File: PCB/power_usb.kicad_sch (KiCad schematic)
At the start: 29 parts, among them J1 USB_C_Receptacle, U1 LP2985-3.3, U3 CP2102N-A02-GQFN24, U5 LP2985-3.3

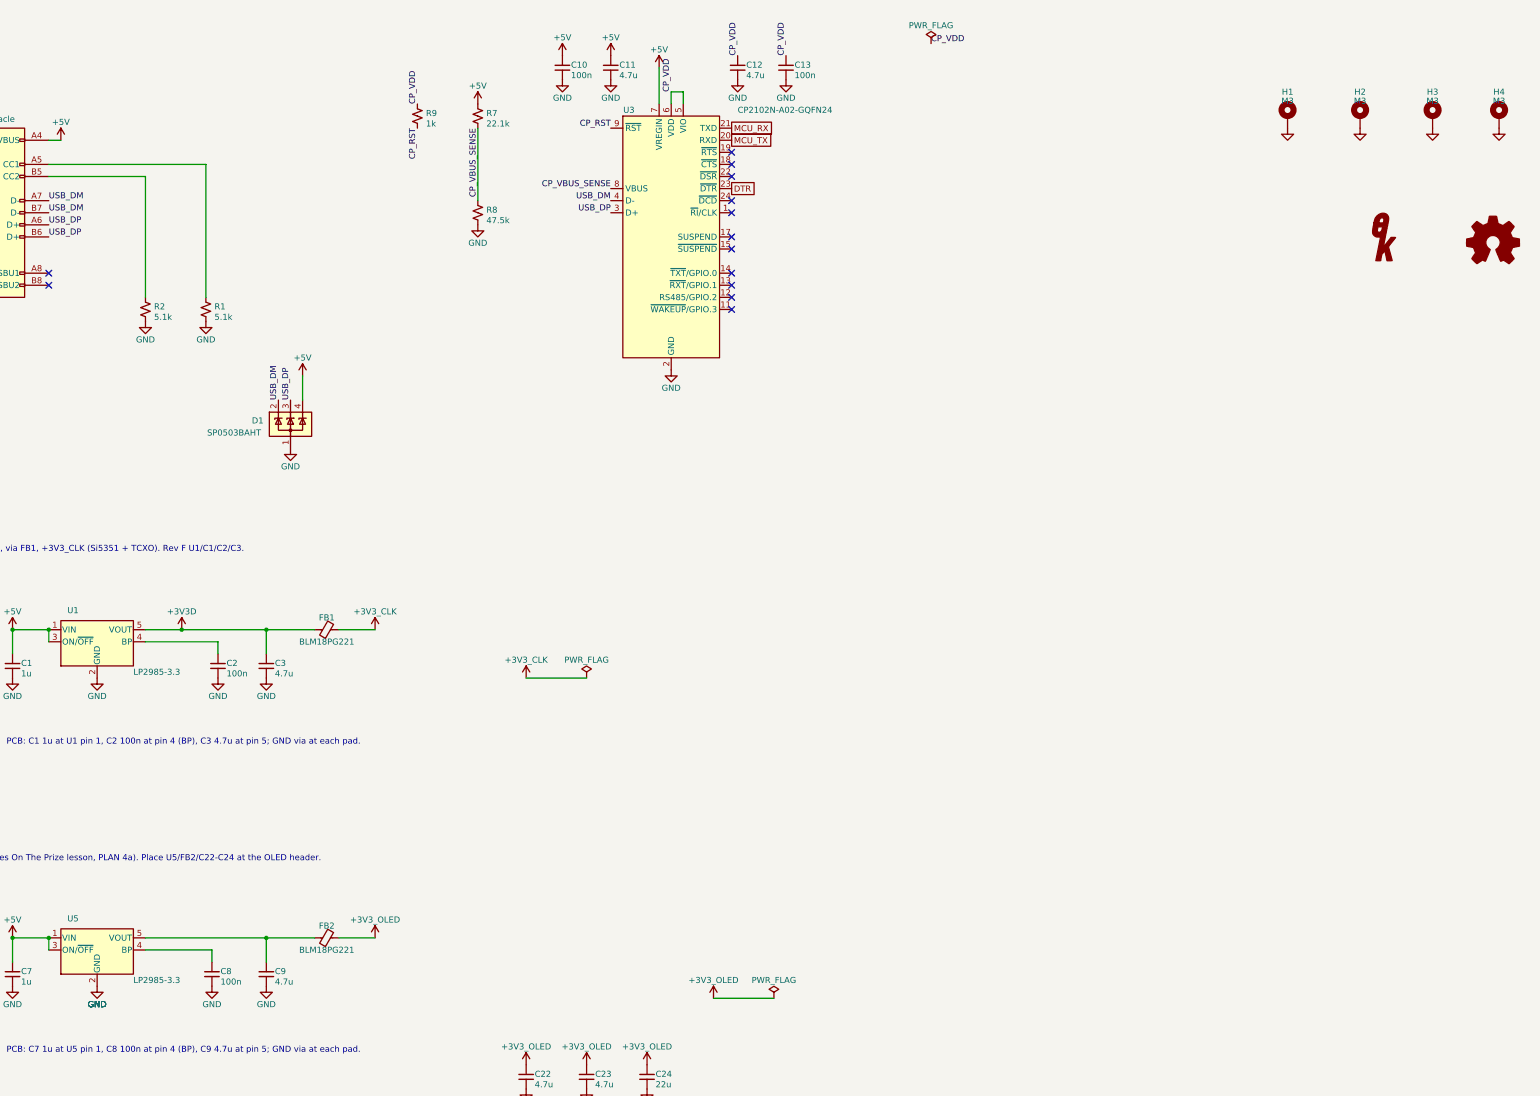
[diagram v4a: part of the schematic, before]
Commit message: SH1: DNP RF shield solder fence (GND), OSHW logo footprint
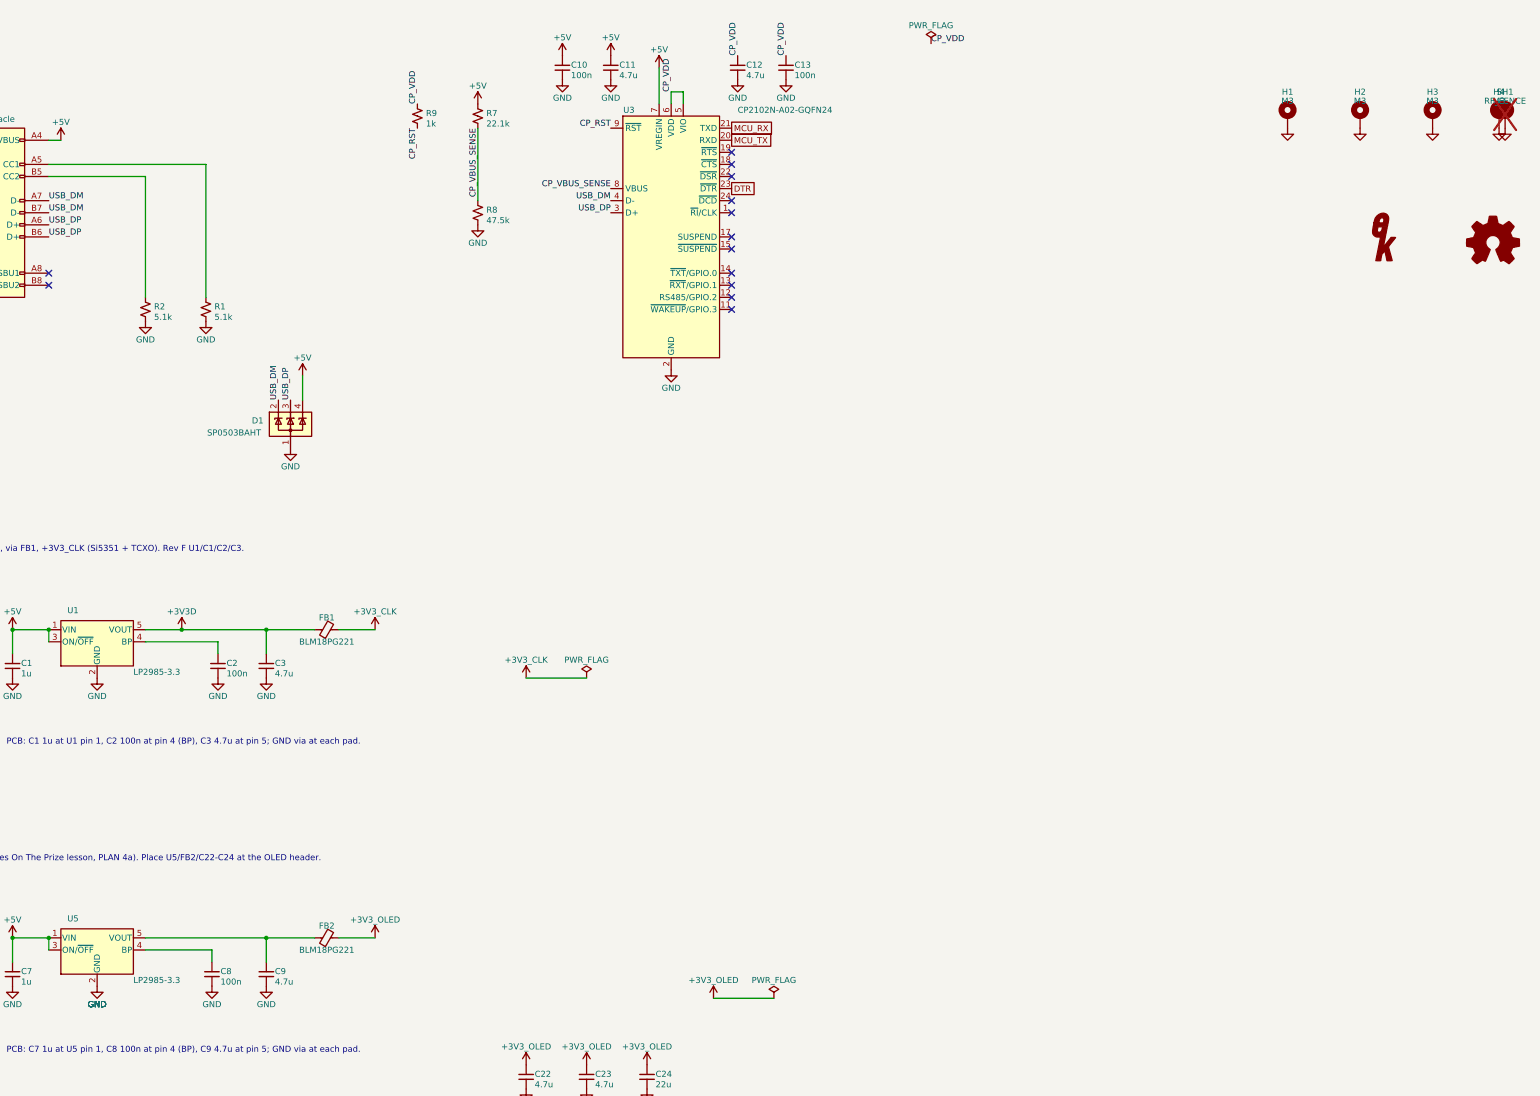
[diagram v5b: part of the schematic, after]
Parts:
- added SH1: RF_FENCE, EtherkitKicadLibrary:RF_Fence_42x33.5mm, symbol Mechanical:MountingHole_Pad
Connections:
- net GND: now also SH1.1
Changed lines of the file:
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@@
+	)
+	(symbol
+		(lib_id "Mechanical:MountingHole_Pad")
+		(at 365.76 59.69 0)
+		(unit 1)
+		(body_style 1)
+		(exclude_from_sim no)
+		(in_bom no)
+		(on_board yes)
+		(in_pos_files no)
+		(dnp yes)
+		(property "Reference" "SH1"
+			(at 365.76 54.61 0)
+			(show_name no)
+			(do_not_autoplace no)
+			(effects
+				(font
+					(size 1.27 1.27)
+				)
+			)
+		)
+		(property "Value" "RF_FENCE"
+			(at 365.76 56.515 0)
+			(show_name no)
+			(do_not_autoplace no)
+			(effects
+				(font
+					(size 1.27 1.27)
+				)
+			)
+		)
+		(property "Footprint" "EtherkitKicadLibrary:RF_Fence_42x33.5mm"
+			(at 365.76 59.69 0)
+			(hide yes)
+			(show_name no)
+			(do_not_autoplace no)
+			(effects
+				(font
+					(size 1.27 1.27)
+				)
+			)
+		)
+		(property "Datasheet" ""
+			(at 365.76 59.69 0)
+			(hide yes)
+			(show_name no)
+			(do_not_autoplace no)
+			(effects
+				(font
+					(size 1.27 1.27)
+				)
+			)
+		)
+		(property "Description" "DNP RF shield solder fence (42x33.5 mm, 1 mm GND strip) for a user-cut tin-plate can over Si5351/TCXO/LPFs; not in BOM"
+			(at 365.76 59.69 0)
+			(hide yes)
+			(show_name no)
+			(do_not_autoplace no)
+			(effects
+				(font
+					(size 1.27 1.27)
+				)
+			)
+		)
+		(pin "1"
+		)
+		(instances
+			(project "Si5351AVFO"
+				(path "/a0000000-0000-4000-8000-000000000001/b0000000-0000-4000-8000-000000000002"
+					(reference "SH1")
+					(unit 1)
+				)
+			)
+		)
+	)
+	(symbol
+		(lib_id "power:GND")
+		(at 365.76 62.23 0)
+		(unit 1)
+		(body_style 1)
+		(exclude_from_sim no)
+		(in_bom no)
+		(on_board yes)
+		(in_pos_files yes)
+		(dnp no)
+		(property "Reference" "#PWR910"
+			(at 365.76 62.23 0)
+			(hide yes)
+			(show_name no)
+			(do_not_autoplace no)
+			(effects
+				(font
+					(size 1.27 1.27)
+				)
+			)
+		)
+		(property "Value" "GND"
+			(at 69.85 246.38 0)
+			(show_name no)
+			(do_not_autoplace no)
+			(effects
+				(font
+					(size 1.27 1.27)
+				)
+			)
+		)
+		(property "Footprint" ""
+			(at 365.76 62.23 0)
+			(hide yes)
+			(show_name no)
+			(do_not_autoplace no)
+			(effects
+				(font
+					(size 1.27 1.27)
+				)
+			)
+		)
+		(property "Datasheet" ""
+			(at 365.76 62.23 0)
+			(hide yes)
+			(show_name no)
+			(do_not_autoplace no)
+			(effects
+				(font
+					(size 1.27 1.27)
+				)
+			)
+		)
+		(property "Description" ""
+			(at 365.76 62.23 0)
+			(show_name no)
+			(do_not_autoplace no)
+			(effects
+				(font
+					(size 1.27 1.27)
+				)
+			)
+		)
+		(pin "1"
+		)
+		(instances
+			(project "Si5351AVFO"
+				(path "/a0000000-0000-4000-8000-000000000001/b0000000-0000-4000-8000-000000000002"
+					(reference "#PWR910")
+					(unit 1)
+				)
+			)
+		)
 	)
 	(symbol

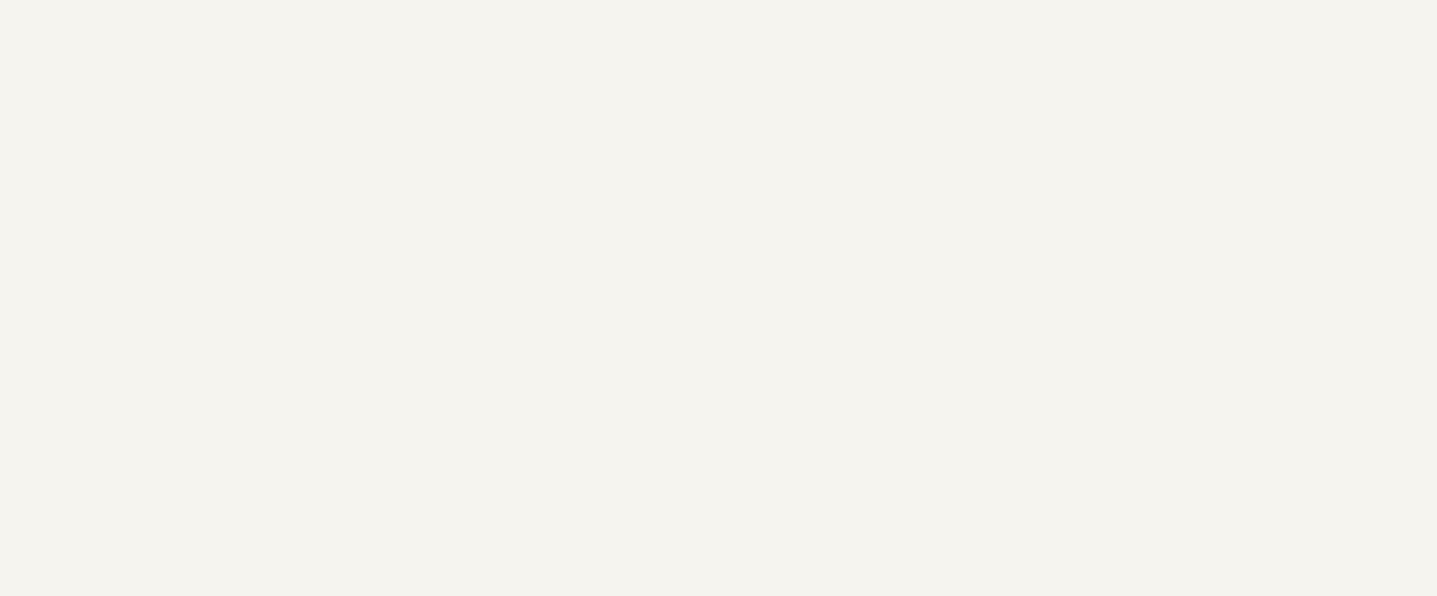
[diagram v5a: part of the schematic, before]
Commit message: Test points TP1-TP8 (GND x2, +5V, +3V3D, +3V3_CLK, +3V3_OLED, I2C_SCL/SDA) on B.Cu, 1.5 mm SMD, excluded from BOM/CPL; no RF nets. JLC fab outputs (tools/export_fab.sh -> PCB/production). ERC 0, DRC only the 15 accepted SMA edge hits
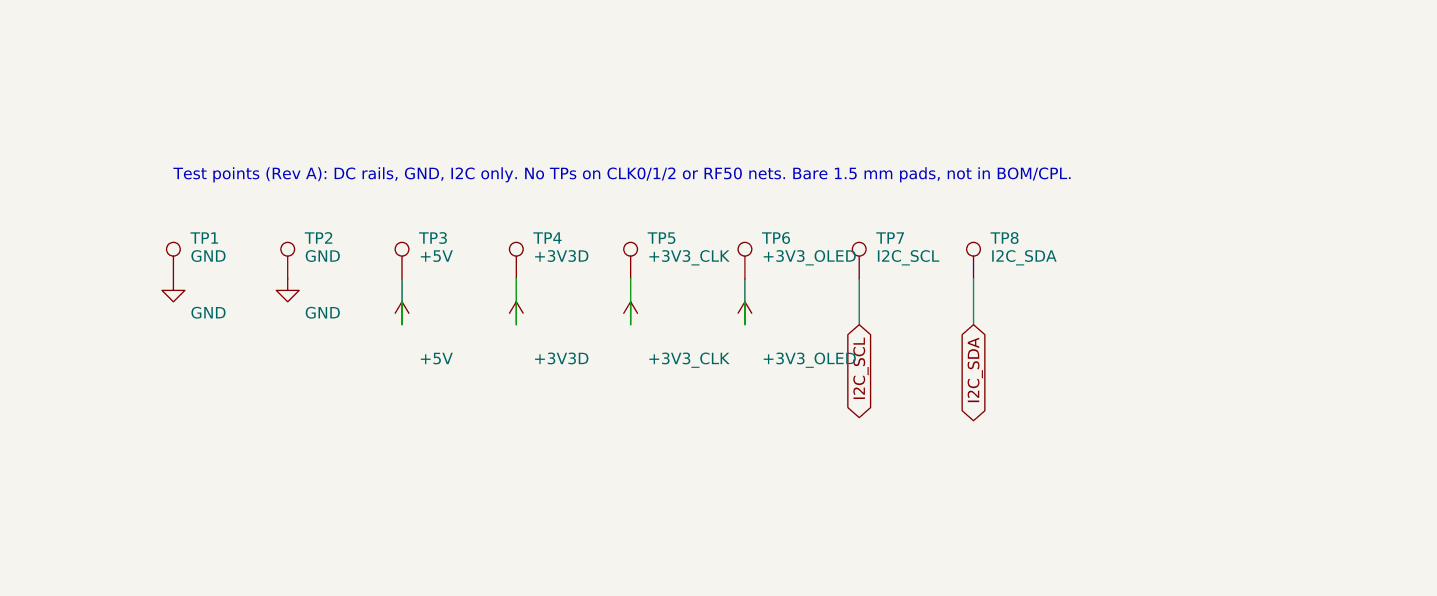
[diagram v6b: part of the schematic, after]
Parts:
- added TP1, TP2: GND, TestPoint:TestPoint_Pad_D1.5mm, symbol Connector:TestPoint
- added TP3: +5V, TestPoint:TestPoint_Pad_D1.5mm, symbol Connector:TestPoint
- added TP4: +3V3D, TestPoint:TestPoint_Pad_D1.5mm, symbol Connector:TestPoint
- added TP5: +3V3_CLK, TestPoint:TestPoint_Pad_D1.5mm, symbol Connector:TestPoint
- added TP6: +3V3_OLED, TestPoint:TestPoint_Pad_D1.5mm, symbol Connector:TestPoint
- added TP7: I2C_SCL, TestPoint:TestPoint_Pad_D1.5mm, symbol Connector:TestPoint
- added TP8: I2C_SDA, TestPoint:TestPoint_Pad_D1.5mm, symbol Connector:TestPoint
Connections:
- net +3V3D: now also TP4.1
- net +3V3_CLK: now also TP5.1
- net +3V3_OLED: now also TP6.1
- net +5V: now also TP3.1
- net GND: now also TP1.1, TP2.1
- new net I2C_SCL: TP7.1
- new net I2C_SDA: TP8.1
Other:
- note added: "Test points (Rev A): DC rails, GND, I2C only. No TPs on CLK0/1/2 or RF50 nets. Bare 1.5 mm pads, not in BOM/CPL."

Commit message: Basic-part swaps: C11/C12 C1705->C19666 (CL10A475KO8NNNC 16V), R1/R2 C105580->C23186 (0603WAF5101T5E). Board fields synced, ERC 0, DRC 15 accepted SMA hits, fab outputs + schematic PDF regenerated
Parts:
- C11, C12: LCSC C1705 -> C19666; MPN CL10A475KP8NNNC -> CL10A475KO8NNNC
- R1, R2: LCSC C105580 -> C23186; MPN RC0603FR-075K1L -> 0603WAF5101T5E; Manufacturer YAGEO -> UNI-ROYAL
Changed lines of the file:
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@@
 			)
 		)
-		(property "LCSC" "C1705"
+		(property "LCSC" "C19666"
 			(at 204.47 49.53 0)
 			(hide yes)
@@
 			)
 		)
-		(property "MPN" "CL10A475KP8NNNC"
+		(property "MPN" "CL10A475KO8NNNC"
 			(at 204.47 49.53 0)
 			(hide yes)
@@
 			)
 		)
-		(property "LCSC" "C1705"
+		(property "LCSC" "C19666"
 			(at 177.8 49.53 0)
 			(hide yes)
@@
 			)
 		)
-		(property "MPN" "CL10A475KP8NNNC"
+		(property "MPN" "CL10A475KO8NNNC"
 			(at 177.8 49.53 0)
 			(hide yes)
@@
 			)
 		)
-		(property "LCSC" "C105580"
+		(property "LCSC" "C23186"
 			(at 80.01 100.33 0)
 			(hide yes)
@@
 			)
 		)
-		(property "MPN" "RC0603FR-075K1L"
+		(property "MPN" "0603WAF5101T5E"
 			(at 80.01 100.33 0)
 			(hide yes)
@@
 			)
 		)
-		(property "Manufacturer" "YAGEO"
+		(property "Manufacturer" "UNI-ROYAL"
 			(at 80.01 100.33 0)
 			(hide yes)
@@
 			)
 		)
-		(property "LCSC" "C105580"
+		(property "LCSC" "C23186"
 			(at 92.71 100.33 0)
 			(hide yes)
@@
 			)
 		)
-		(property "MPN" "RC0603FR-075K1L"
+		(property "MPN" "0603WAF5101T5E"
 			(at 92.71 100.33 0)
 			(hide yes)
@@
 			)
 		)
-		(property "Manufacturer" "YAGEO"
+		(property "Manufacturer" "UNI-ROYAL"
 			(at 92.71 100.33 0)
 			(hide yes)
